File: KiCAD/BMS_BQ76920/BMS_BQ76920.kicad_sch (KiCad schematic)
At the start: 0 parts

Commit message: BMS
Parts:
- added U1: ~, symbol BMS_Custom:BQ76920
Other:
- company: (none) -> AAA Engineering
- title: (none) -> Li-Ion Battery Management System
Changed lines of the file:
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@@
 	(generator_version "9.0")
 	(paper "A4")
+	(title_block
+		(title "Li-Ion Battery Management System")
+		(rev "1.0")
+		(company "AAA Engineering")
+	)
+	(symbol
+		(lib_id "BMS_Custom:BQ76920")
+		(at 135.89 97.79 0)
+		(unit 1)
+		(exclude_from_sim no)
+		(in_bom yes)
+		(on_board yes)
+		(dnp no)
+		(fields_autoplaced yes)
+		(property "Reference" "U1"
+			(at 135.89 80.01 0)
+			(effects
+				(font
+					(size 1.27 1.27)
+				)
+			)
+		)
+		(property "Value" "~"
+			(at 135.89 82.55 0)
+			(effects
+				(font
+					(size 1.27 1.27)
+				)
+			)
+		)
+		(property "Footprint" ""
+			(at 135.89 97.79 0)
+			(effects
+				(font
+					(size 1.27 1.27)
+				)
+				(hide yes)
+			)
+		)
+		(property "Datasheet" ""
+			(at 135.89 97.79 0)
+			(effects
+				(font
+					(size 1.27 1.27)
+				)
+				(hide yes)
+			)
+		)
+		(property "Description" ""
+			(at 135.89 97.79 0)
+			(effects
+				(font
+					(size 1.27 1.27)
+				)
+				(hide yes)
+			)
+		)
+		(pin "16"
+		)
+		(pin "1"
+		)
+		(pin "7"
+		)
+		(pin "17"
+		)
+		(pin "4"
+		)
+		(pin "3"
+		)
+		(pin "6"
+		)
+		(pin "14"
+		)
+		(pin "8"
+		)
+		(pin "10"
+		)
+		(pin "13"
+		)
+		(pin "2"
+		)
+		(pin "5"
+		)
+		(pin "19"
+		)
+		(pin "11"
+		)
+		(pin "15"
+		)
+		(pin "20"
+		)
+		(pin "9"
+		)
+		(pin "18"
+		)
+		(pin "12"
+		)
+		(instances
+			(project ""
+				(path "/dcb53800-8b85-425e-952c-2cefee05727b"
+					(reference "U1")
+					(unit 1)
+				)
+			)
+		)
+	)
 	(sheet_instances
 		(path "/"

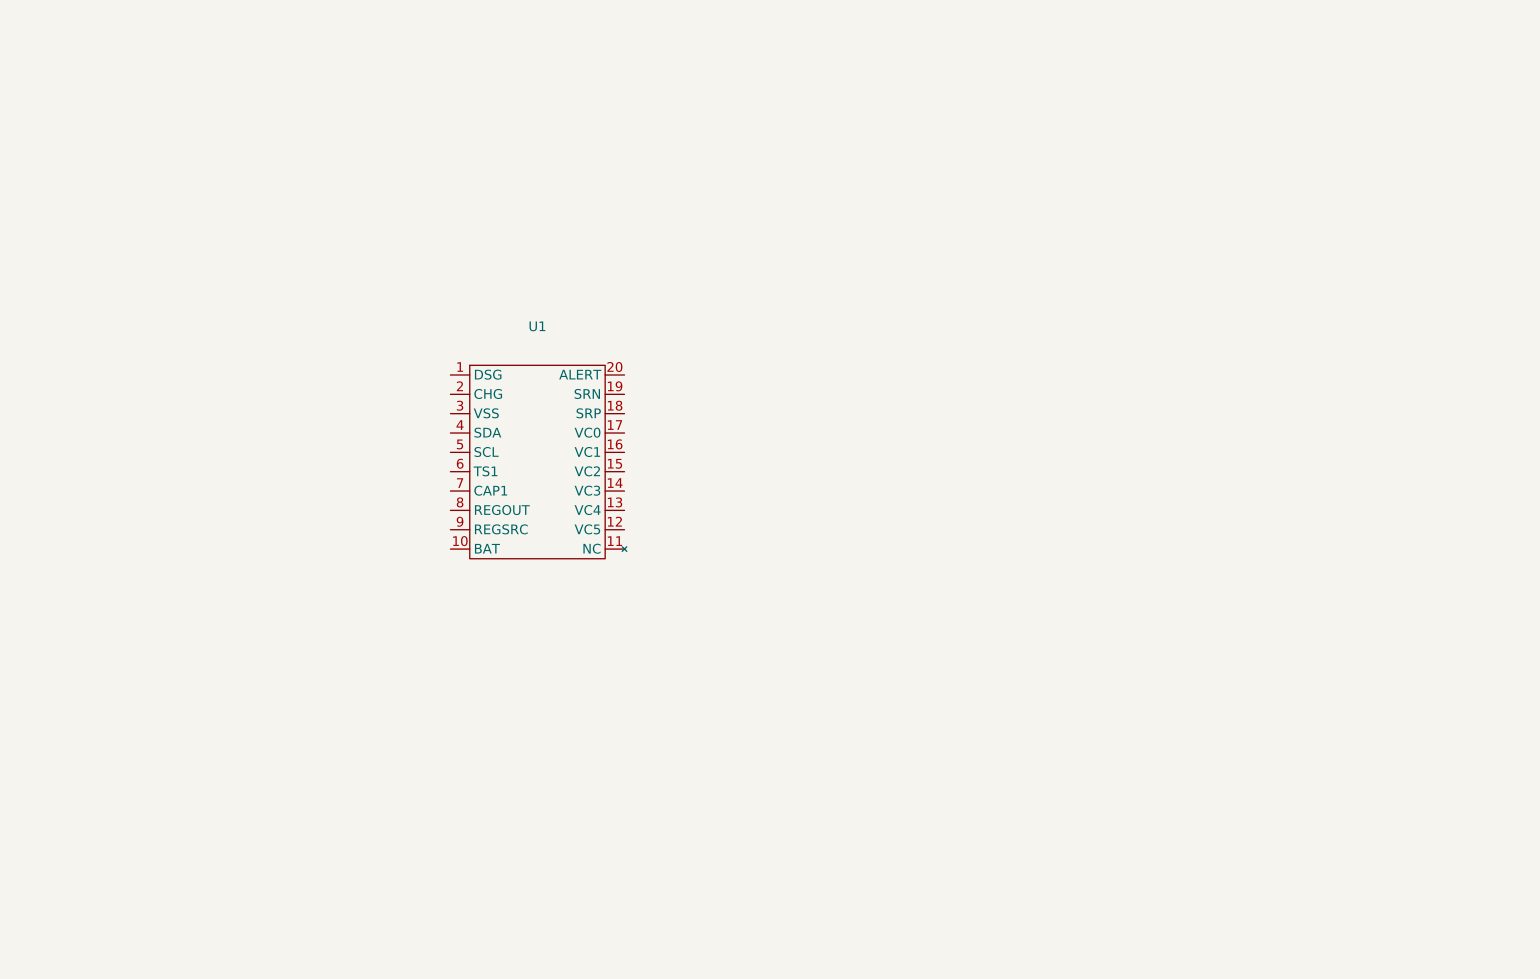
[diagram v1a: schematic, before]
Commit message: Arrange power path - Q1 Q2 Rsns correct orientation and layout
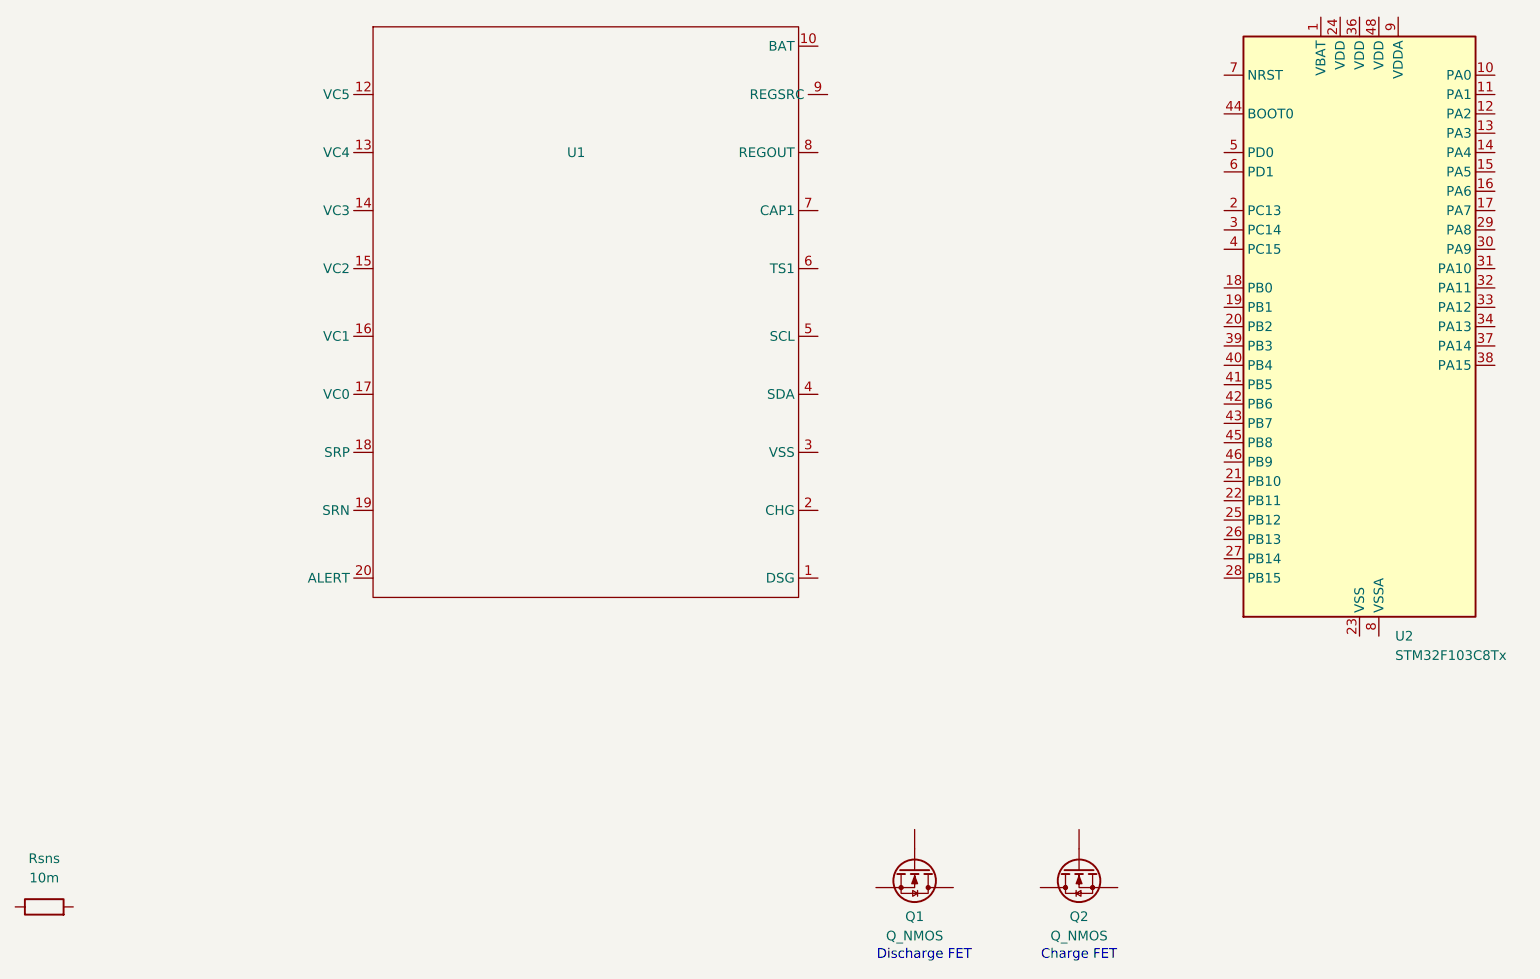
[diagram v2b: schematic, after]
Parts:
- added Q1, Q2: Q_NMOS, symbol Device:Q_NMOS
- added Rsns: 10m, symbol Device:R
- added U2: STM32F103C8Tx, Package_QFP:LQFP-48_7x7mm_P0.5mm, symbol MCU_ST_STM32F1:STM32F103C8Tx
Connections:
- new net: U2.23 (VSS), U2.35 (VSS), U2.47 (VSS)
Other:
- note added: "Charge FET"
- note added: "Discharge FET"
